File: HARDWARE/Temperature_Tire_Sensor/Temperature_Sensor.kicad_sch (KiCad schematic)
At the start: 4 parts

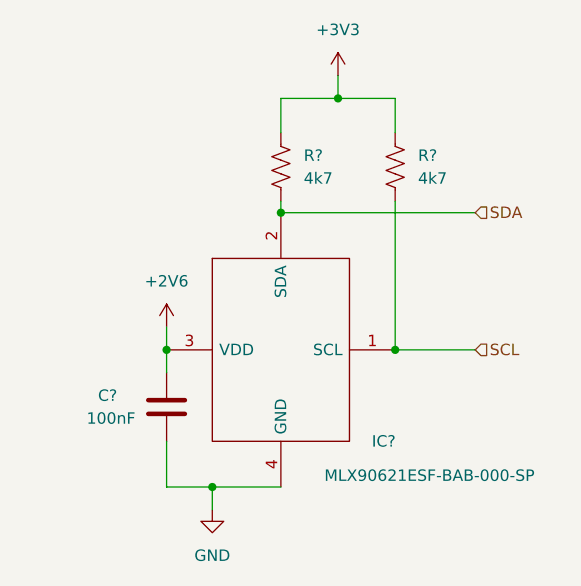
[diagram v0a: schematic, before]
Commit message: Changed the used type of labels and added power flags
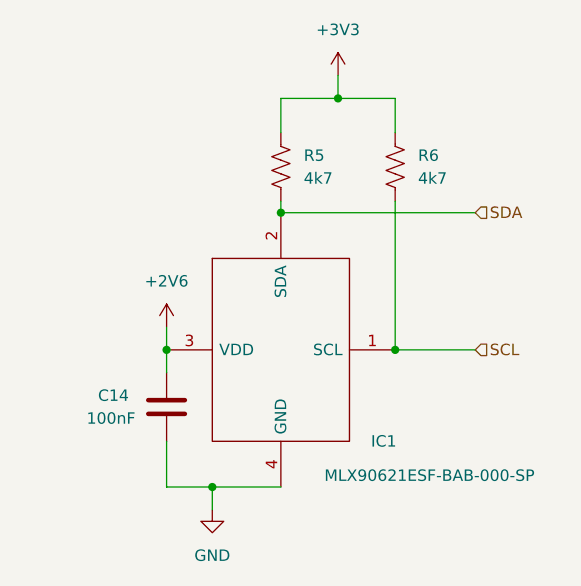
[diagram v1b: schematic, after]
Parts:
- gave numbers to parts that had none: 4
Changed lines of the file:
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@@
   (symbol (lib_id "power:+2V6") (at 130.81 97.79 0) (unit 1)
     (in_bom yes) (on_board yes) (fields_autoplaced)
-    (property "Reference" "#PWR?" (id 0) (at 130.81 101.6 0)
+    (property "Reference" "#PWR018" (id 0) (at 130.81 101.6 0)
       (effects (font (size 1.27 1.27)) hide)
     )
@@
   (symbol (lib_id "Device:R_US") (at 156.21 80.01 0) (unit 1)
     (in_bom yes) (on_board yes) (fields_autoplaced)
-    (property "Reference" "R?" (id 0) (at 158.75 78.7399 0)
+    (property "Reference" "R6" (id 0) (at 158.75 78.7399 0)
       (effects (font (size 1.27 1.27)) (justify left))
     )
@@
   (symbol (lib_id "power:GND") (at 135.89 118.11 0) (unit 1)
     (in_bom yes) (on_board yes) (fields_autoplaced)
-    (property "Reference" "#PWR?" (id 0) (at 135.89 124.46 0)
+    (property "Reference" "#PWR019" (id 0) (at 135.89 124.46 0)
       (effects (font (size 1.27 1.27)) hide)
     )
@@
   (symbol (lib_id "power:+3V3") (at 149.86 69.85 0) (unit 1)
     (in_bom yes) (on_board yes) (fields_autoplaced)
-    (property "Reference" "#PWR?" (id 0) (at 149.86 73.66 0)
+    (property "Reference" "#PWR020" (id 0) (at 149.86 73.66 0)
       (effects (font (size 1.27 1.27)) hide)
     )
@@
   (symbol (lib_id "Device:R_US") (at 143.51 80.01 0) (unit 1)
     (in_bom yes) (on_board yes) (fields_autoplaced)
-    (property "Reference" "R?" (id 0) (at 146.05 78.7399 0)
+    (property "Reference" "R5" (id 0) (at 146.05 78.7399 0)
       (effects (font (size 1.27 1.27)) (justify left))
     )
@@
   (symbol (lib_id "MLX90621ESF-BAB-000-SP:MLX90621ESF-BAB-000-SP") (at 130.81 100.33 0) (unit 1)
     (in_bom yes) (on_board yes)
-    (property "Reference" "IC?" (id 0) (at 154.94 110.49 0))
+    (property "Reference" "IC1" (id 0) (at 154.94 110.49 0))
     (property "Value" "MLX90621ESF-BAB-000-SP" (id 1) (at 160.02 114.3 0))
     (property "Footprint" "MLX90621ESFBAB000SP" (id 2) (at 152.4 90.17 0)
@@
   (symbol (lib_id "Device:C") (at 130.81 106.68 0) (unit 1)
     (in_bom yes) (on_board yes)
-    (property "Reference" "C?" (id 0) (at 123.19 105.41 0)
+    (property "Reference" "C14" (id 0) (at 123.19 105.41 0)
       (effects (font (size 1.27 1.27)) (justify left))
     )

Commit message: Added all of the footprints
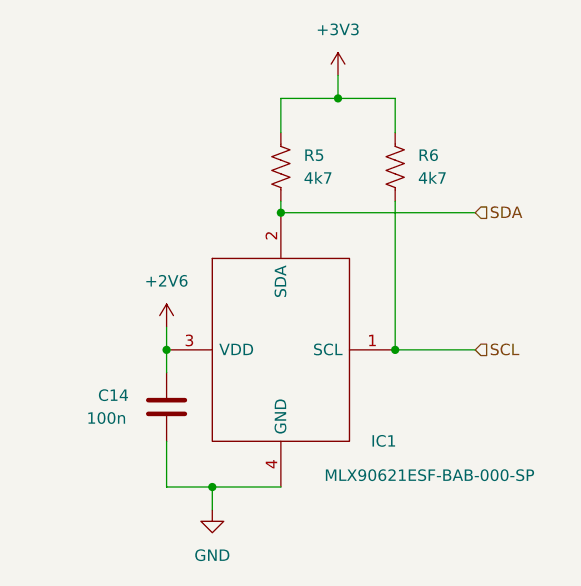
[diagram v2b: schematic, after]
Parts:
- C14: value 100nF -> 100n; footprint (none) -> Capacitor_SMD:C_0603_1608Metric
- IC1: footprint MLX90621ESFBAB000SP -> MLX:MLX90621ESFBAB000SP
- R5, R6: footprint (none) -> Resistor_SMD:R_0603_1608Metric
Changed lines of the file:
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@@
       (effects (font (size 1.27 1.27)) (justify left))
     )
-    (property "Footprint" "" (id 2) (at 157.226 80.264 90)
+    (property "Footprint" "Resistor_SMD:R_0603_1608Metric" (id 2) (at 157.226 80.264 90)
       (effects (font (size 1.27 1.27)) hide)
     )
@@
       (effects (font (size 1.27 1.27)) (justify left))
     )
-    (property "Footprint" "" (id 2) (at 144.526 80.264 90)
+    (property "Footprint" "Resistor_SMD:R_0603_1608Metric" (id 2) (at 144.526 80.264 90)
       (effects (font (size 1.27 1.27)) hide)
     )
@@
     (property "Reference" "IC1" (id 0) (at 154.94 110.49 0))
     (property "Value" "MLX90621ESF-BAB-000-SP" (id 1) (at 160.02 114.3 0))
-    (property "Footprint" "MLX90621ESFBAB000SP" (id 2) (at 152.4 90.17 0)
+    (property "Footprint" "MLX:MLX90621ESFBAB000SP" (id 2) (at 152.4 90.17 0)
       (effects (font (size 1.27 1.27)) (justify left) hide)
     )
@@
       (effects (font (size 1.27 1.27)) (justify left))
     )
-    (property "Value" "100nF" (id 1) (at 121.92 107.95 0)
+    (property "Value" "100n" (id 1) (at 121.92 107.95 0)
       (effects (font (size 1.27 1.27)) (justify left))
     )
-    (property "Footprint" "" (id 2) (at 131.7752 110.49 0)
+    (property "Footprint" "Capacitor_SMD:C_0603_1608Metric" (id 2) (at 131.7752 110.49 0)
       (effects (font (size 1.27 1.27)) hide)
     )

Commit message: Power planes has been added
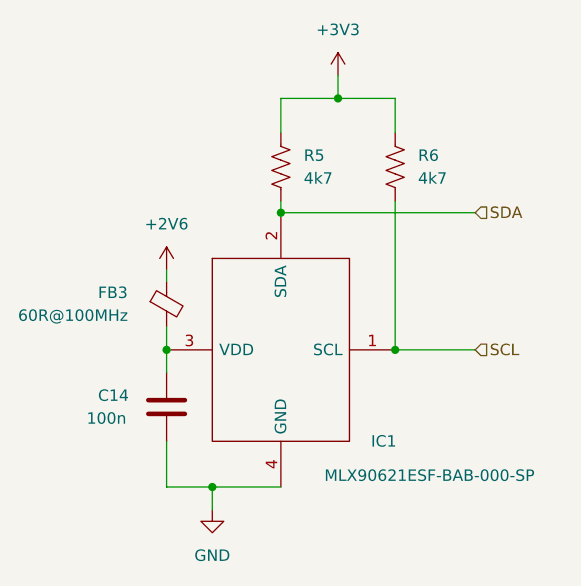
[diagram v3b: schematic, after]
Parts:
- added FB3: 60R@100MHz, Inductor_SMD:L_0603_1608Metric, symbol Device:FerriteBead_Small
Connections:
- net +2V6: now also FB3.1; no longer C14.1, IC1.3 (VDD)
- new net: C14.1, FB3.2, IC1.3 (VDD)
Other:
- title: (none) -> Temperature sensor
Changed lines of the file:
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@@
 (kicad_sch (version 20211123) (generator eeschema)
   (paper "A4")
+  (title_block
+    (title "Temperature sensor")
+  )
   (junction (at 149.86 72.39) (diameter 0) (color 0 0 0 0)
   )
@@
   )
   (wire (pts (xy 130.81 97.79) (xy 130.81 100.33))
+    (stroke (width 0) (type default) (color 0 0 0 0))
+  )
+  (wire (pts (xy 130.81 91.44) (xy 130.81 92.71))
     (stroke (width 0) (type default) (color 0 0 0 0))
   )
@@
     (effects (font (size 1.27 1.27)) (justify left))
   )
-  (symbol (lib_id "power:+2V6") (at 130.81 97.79 0) (unit 1)
-    (in_bom yes) (on_board yes) (fields_autoplaced)
-    (property "Reference" "#PWR018" (id 0) (at 130.81 101.6 0)
+  (symbol (lib_id "Device:FerriteBead_Small") (at 130.81 95.25 0) (unit 1)
+    (in_bom yes) (on_board yes)
+    (property "Reference" "FB3" (id 0) (at 123.19 93.98 0)
+      (effects (font (size 1.27 1.27)) (justify left))
+    )
+    (property "Value" "60R@100MHz" (id 1) (at 114.3 96.52 0)
+      (effects (font (size 1.27 1.27)) (justify left))
+    )
+    (property "Footprint" "Inductor_SMD:L_0603_1608Metric" (id 2) (at 129.032 95.25 90)
       (effects (font (size 1.27 1.27)) hide)
     )
-    (property "Value" "+2V6" (id 1) (at 130.81 92.71 0))
-    (property "Footprint" "" (id 2) (at 130.81 97.79 0)
-      (effects (font (size 1.27 1.27)) hide)
-    )
-    (property "Datasheet" "" (id 3) (at 130.81 97.79 0)
+    (property "Datasheet" "~" (id 3) (at 130.81 95.25 0)
       (effects (font (size 1.27 1.27)) hide)
     )
     (pin "1")
+    (pin "2")
   )
   (symbol (lib_id "Device:R_US") (at 156.21 80.01 0) (unit 1)
@@
     (pin "2")
   )
+  (symbol (lib_id "power:+2V6") (at 130.81 91.44 0) (unit 1)
+    (in_bom yes) (on_board yes) (fields_autoplaced)
+    (property "Reference" "#PWR07" (id 0) (at 130.81 95.25 0)
+      (effects (font (size 1.27 1.27)) hide)
+    )
+    (property "Value" "+2V6" (id 1) (at 130.81 86.36 0))
+    (property "Footprint" "" (id 2) (at 130.81 91.44 0)
+      (effects (font (size 1.27 1.27)) hide)
+    )
+    (property "Datasheet" "" (id 3) (at 130.81 91.44 0)
+      (effects (font (size 1.27 1.27)) hide)
+    )
+    (pin "1")
+  )
   (symbol (lib_id "MLX90621ESF-BAB-000-SP:MLX90621ESF-BAB-000-SP") (at 130.81 100.33 0) (unit 1)
